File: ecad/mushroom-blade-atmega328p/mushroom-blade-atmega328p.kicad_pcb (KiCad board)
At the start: 2 copper layers, 25 x 98 mm, 96 parts, among them J1 USB-C PORT, J2 ICSP, J3 BACKPLANE, J4 RASPBERRY PI GPIO, Q1 AO3400A, Q2 AO3400A, Q3 SI2301CDS-T1-GE3, Q4 AO3400A, SW1 RESET, SW2 SW_DIP_x06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

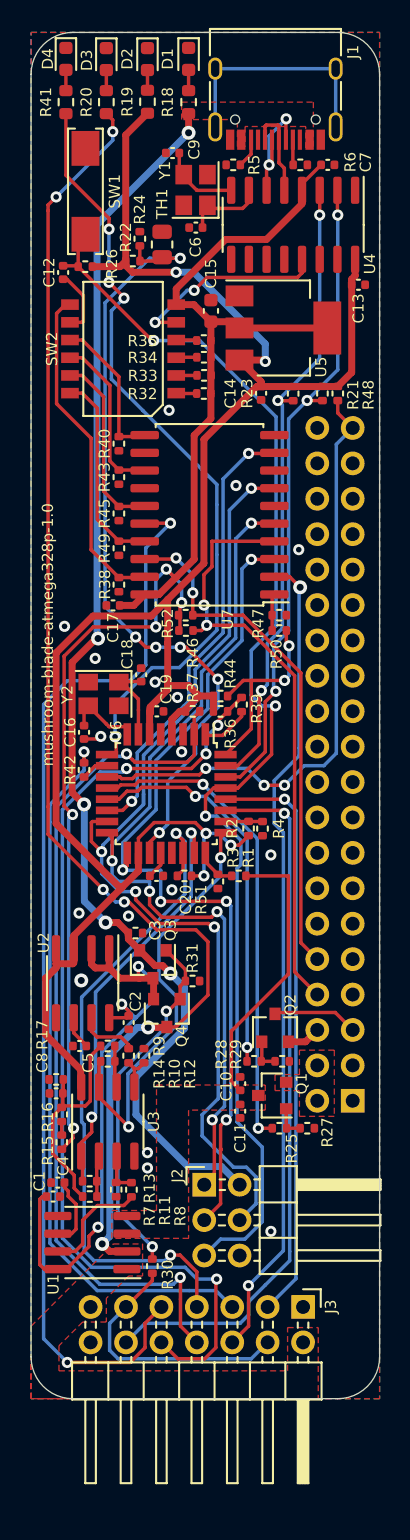
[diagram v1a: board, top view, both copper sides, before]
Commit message: Move ICSP header by extending PCB
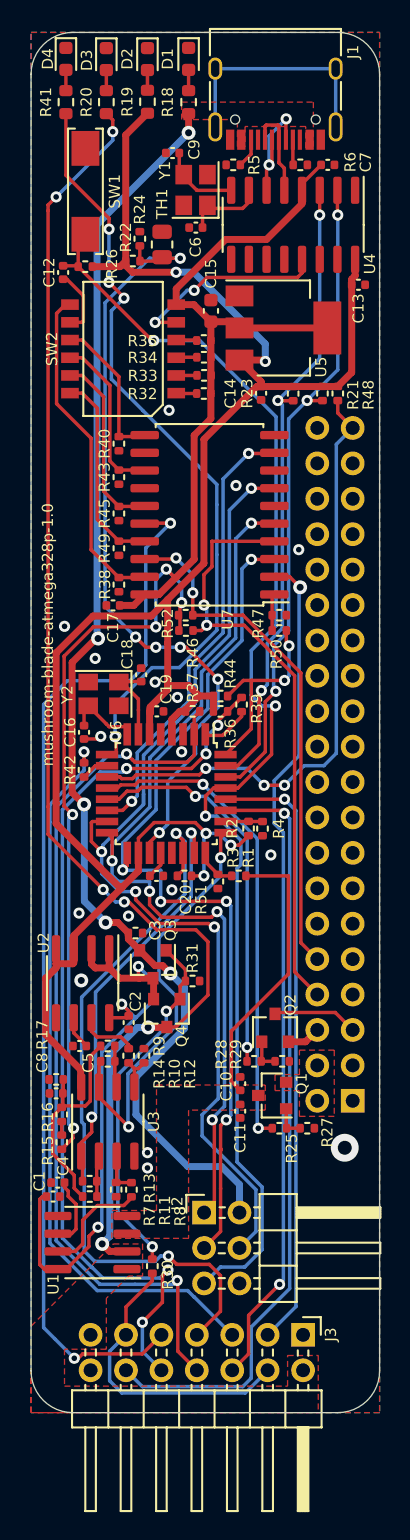
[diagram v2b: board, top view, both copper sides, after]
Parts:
- moved J2 2.00 mm to (99.9, 134.7)
- moved J3 2.00 mm to (107.0, 143.4)
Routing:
- net SDA: track 51.3 -> 55.8 mm
- net FANPWM: track 69.9 -> 65.5 mm, vias 4 -> 5
- net POWTMP: track 48.4 -> 52.6 mm
- net STX: track 78.6 -> 76.0 mm
- net VIN: track 18.9 -> 21.4 mm
- net SCLK: track 62.8 -> 64.8 mm
- net MISO: track 63.8 -> 65.8 mm
- net SCL: track 41.8 -> 43.8 mm
- net 5VEXT: track 90.8 -> 92.8 mm
- net RESET: track 92.7 -> 94.7 mm
- net SRX: track 58.9 -> 60.9 mm
- net FANFDB: track 61.9 -> 63.5 mm
- net MOSI: track 72.3 -> 73.7 mm
- net FANDCC: track 52.2 -> 53.1 mm
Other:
- board size 25 x 98 mm -> 25 x 99 mm
